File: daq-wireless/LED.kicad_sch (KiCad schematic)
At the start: 6 parts

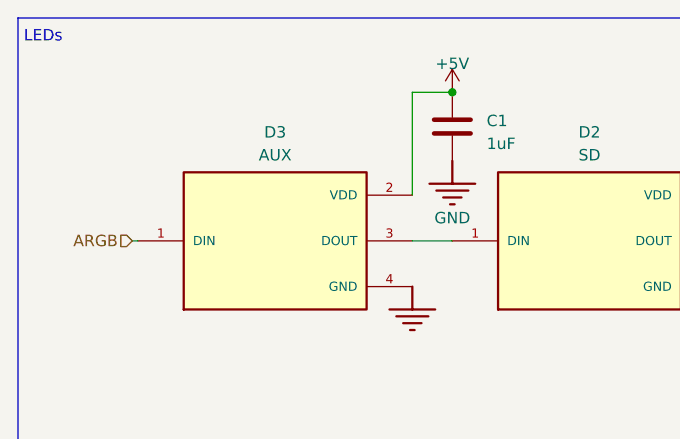
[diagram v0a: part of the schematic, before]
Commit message: Critical ESPdaq fix
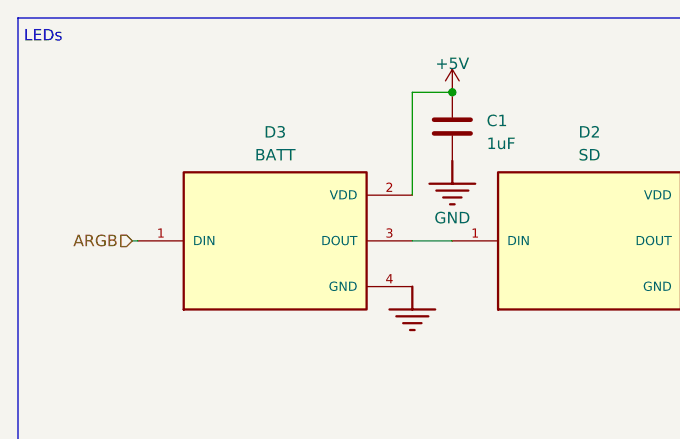
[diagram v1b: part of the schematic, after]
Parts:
- D3: value AUX -> BATT
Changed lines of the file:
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@@
       (effects (font (size 1.27 1.27)))
     )
-    (property "Value" "AUX" (at 86.995 63.5 0)
+    (property "Value" "BATT" (at 86.995 63.5 0)
       (effects (font (size 1.27 1.27)))
     )
